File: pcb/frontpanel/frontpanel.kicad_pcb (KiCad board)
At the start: 2 copper layers, 175.8 x 64 mm, 9 parts, among them J1 xx, J2 xx, J3 xx, J4 xx

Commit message: [pcb] update
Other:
- outline, holes or cut-outs redrawn
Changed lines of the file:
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@@
     (property "ki_keywords" "LED diode")
     (attr smd)
-    (fp_text reference "D1" (at 0 1.65) (layer "B.SilkS")
+    (fp_text reference "D1" (at 0 1.8) (layer "B.SilkS")
         (effects (font (size 1 1) (thickness 0.15)) (justify mirror))
     )
@@
     (property "ki_keywords" "LED diode")
     (attr smd)
-    (fp_text reference "D4" (at 0 1.65) (layer "B.SilkS")
+    (fp_text reference "D4" (at 0 1.725) (layer "B.SilkS")
         (effects (font (size 1 1) (thickness 0.15)) (justify mirror))
     )
@@
     (property "ki_keywords" "LED diode")
     (attr smd)
-    (fp_text reference "D3" (at 0 1.65) (layer "B.SilkS")
+    (fp_text reference "D3" (at 0 1.75) (layer "B.SilkS")
         (effects (font (size 1 1) (thickness 0.15)) (justify mirror))
     )
@@
     (property "ki_keywords" "R res resistor")
     (attr smd)
-    (fp_text reference "R1" (at 0 1.43) (layer "B.SilkS")
+    (fp_text reference "R1" (at 0 1.5) (layer "B.SilkS")
         (effects (font (size 1 1) (thickness 0.15)) (justify mirror))
     )
@@
     (property "ki_keywords" "LED diode")
     (attr smd)
-    (fp_text reference "D2" (at 0 1.65) (layer "B.SilkS")
+    (fp_text reference "D2" (at 0 1.725) (layer "B.SilkS")
         (effects (font (size 1 1) (thickness 0.15)) (justify mirror))
     )
@@
   (gr_line (start 215.625 139.094185) (end 73.895815 139.094185)
     (stroke (width 0.05) (type default)) (layer "Edge.Cuts"))
+  (gr_circle (center 97.475 90.8) (end 99.975 90.8)
+    (stroke (width 0.05) (type default)) (fill none) (layer "Edge.Cuts"))
+  (gr_circle (center 193.175 106.75) (end 195.675 106.75)
+    (stroke (width 0.05) (type default)) (fill none) (layer "Edge.Cuts"))
+  (gr_circle (center 97.475 122.8) (end 99.975 122.8)
+    (stroke (width 0.05) (type default)) (fill none) (layer "Edge.Cuts"))
   (gr_arc (start 232.625 122.094185) (mid 227.645821 134.11501) (end 215.625 139.094185)
     (stroke (width 0.05) (type default)) (layer "Edge.Cuts"))
   (gr_arc (start 56.875 92.115) (mid 61.854185 80.094185) (end 73.875 75.115)
     (stroke (width 0.05) (type default)) (layer "Edge.Cuts"))
+  (gr_circle (center 193.375 122.8) (end 195.875 122.8)
+    (stroke (width 0.05) (type default)) (fill none) (layer "Edge.Cuts"))
   (gr_line (start 56.875 92.115) (end 56.895815 122.094185)
     (stroke (width 0.05) (type default)) (layer "Edge.Cuts"))
+  (gr_circle (center 193.175 90.8) (end 195.675 90.8)
+    (stroke (width 0.05) (type default)) (fill none) (layer "Edge.Cuts"))
   (gr_arc (start 215.625 75.115) (mid 227.645815 80.094185) (end 232.625 92.115)
     (stroke (width 0.05) (type default)) (layer "Edge.Cuts"))
+  (gr_circle (center 97.5 106.725) (end 100 106.725)
+    (stroke (width 0.05) (type default)) (fill none) (layer "Edge.Cuts"))
   (gr_rect (start 120.925 94.875) (end 169.525 118.675)
     (stroke (width 0.1) (type default)) (fill none) (layer "Edge.Cuts"))
@@
   )
   (dimension (type aligned) (layer "User.1")
+    (pts (xy 193.275 106.8) (xy 193.275 90.8))
+    (height -13.5)
+    (gr_text "16.0000 mm" (at 178.625 98.8 90) (layer "User.1")
+      (effects (font (size 1 1) (thickness 0.15)))
+    )
+    (format (prefix "") (suffix "") (units 3) (units_format 1) (precision 4))
+    (style (thickness 0.1) (arrow_length 1.27) (text_position_mode 0) (extension_height 0.58642) (extension_offset 0.5) keep_text_aligned)
+  )
+  (dimension (type aligned) (layer "User.1")
     (pts (xy 216.725 82.775) (xy 216.715 106.765))
     (height 169.76259)
@@
   )
   (dimension (type aligned) (layer "User.1")
+    (pts (xy 97.475 122.8) (xy 97.475 106.8))
+    (height -13.5)
+    (gr_text "16.0000 mm" (at 82.825 114.8 90) (layer "User.1")
+      (effects (font (size 1 1) (thickness 0.15)))
+    )
+    (format (prefix "") (suffix "") (units 3) (units_format 1) (precision 4))
+    (style (thickness 0.1) (arrow_length 1.27) (text_position_mode 0) (extension_height 0.58642) (extension_offset 0.5) keep_text_aligned)
+  )
+  (dimension (type aligned) (layer "User.1")
     (pts (xy 73.875 83.115) (xy 81.875 83.115))
     (height -1.75)
@@
   )
   (dimension (type aligned) (layer "User.1")
+    (pts (xy 216.865 106.79) (xy 193.175 106.8))
+    (height 17.469515)
+    (gr_text "23.6900 mm" (at 205.012141 88.175487 0.02418563787) (layer "User.1")
+      (effects (font (size 1 1) (thickness 0.15)))
+    )
+    (format (prefix "") (suffix "") (units 3) (units_format 1) (precision 4))
+    (style (thickness 0.1) (arrow_length 1.27) (text_position_mode 0) (extension_height 0.58642) (extension_offset 0.5) keep_text_aligned)
+  )
+  (dimension (type aligned) (layer "User.1")
     (pts (xy 73.885 131.115) (xy 81.885 131.115))
     (height 3.25)
@@
   )
   (dimension (type aligned) (layer "User.1")
+    (pts (xy 73.875 106.7) (xy 97.475 106.7))
+    (height -5.975)
+    (gr_text "23.6000 mm" (at 85.675 99.575) (layer "User.1")
+      (effects (font (size 1 1) (thickness 0.15)))
+    )
+    (format (prefix "") (suffix "") (units 3) (units_format 1) (precision 4))
+    (style (thickness 0.1) (arrow_length 1.27) (text_position_mode 0) (extension_height 0.58642) (extension_offset 0.5) keep_text_aligned)
+  )
+  (dimension (type aligned) (layer "User.1")
+    (pts (xy 193.275 122.8) (xy 193.275 106.8))
+    (height -13.5)
+    (gr_text "16.0000 mm" (at 178.625 114.8 90) (layer "User.1")
+      (effects (font (size 1 1) (thickness 0.15)))
+    )
+    (format (prefix "") (suffix "") (units 3) (units_format 1) (precision 4))
+    (style (thickness 0.1) (arrow_length 1.27) (text_position_mode 0) (extension_height 0.58642) (extension_offset 0.5) keep_text_aligned)
+  )
+  (dimension (type aligned) (layer "User.1")
     (pts (xy 223.715 82.765) (xy 66.715 82.765))
     (height 20.24)
     (gr_text "157.0000 mm" (at 145.215 61.375) (layer "User.1")
+      (effects (font (size 1 1) (thickness 0.15)))
+    )
+    (format (prefix "") (suffix "") (units 3) (units_format 1) (precision 4))
+    (style (thickness 0.1) (arrow_length 1.27) (text_position_mode 0) (extension_height 0.58642) (extension_offset 0.5) keep_text_aligned)
+  )
+  (dimension (type aligned) (layer "User.1")
+    (pts (xy 97.475 106.8) (xy 97.475 90.8))
+    (height -13.5)
+    (gr_text "16.0000 mm" (at 82.825 98.8 90) (layer "User.1")
       (effects (font (size 1 1) (thickness 0.15)))
     )
@@
     (style (thickness 0.1) (arrow_length 1.27) (text_position_mode 0) (extension_height 0.58642) (extension_offset 0.5) keep_text_aligned)
   )
+  (segment (start 121.578928 120.1) (end 111.575 120.1) (width 0.2) (layer "B.Cu") (net 1))
   (segment (start 83.31 128.075) (end 84.6 128.075) (width 0.2) (layer "B.Cu") (net 1))
+  (segment (start 111.575 120.1) (end 105.275 126.4) (width 0.2) (layer "B.Cu") (net 1))
   (segment (start 83.38 82.8) (end 83.38 128.005) (width 0.2) (layer "B.Cu") (net 1))
   (segment (start 86.65 130.125) (end 206.215 130.125) (width 0.2) (layer "B.Cu") (net 1))
-  (segment (start 121.653928 120.025) (end 91.36 120.025) (width 0.2) (layer "B.Cu") (net 1))
-  (segment (start 91.36 120.025) (end 83.31 128.075) (width 0.2) (layer "B.Cu") (net 1))
+  (segment (start 105.275 126.4) (end 84.985 126.4) (width 0.2) (layer "B.Cu") (net 1))
   (segment (start 84.6 128.075) (end 86.65 130.125) (width 0.2) (layer "B.Cu") (net 1))
   (segment (start 207.46 86.125) (end 207.46 131.37) (width 0.2) (layer "B.Cu") (net 1))
   (segment (start 83.38 128.005) (end 83.31 128.075) (width 0.2) (layer "B.Cu") (net 1))
+  (segment (start 121.653928 120.025) (end 121.578928 120.1) (width 0.2) (layer "B.Cu") (net 1))
   (segment (start 206.215 130.125) (end 207.49 131.4) (width 0.2) (layer "B.Cu") (net 1))
   (segment (start 207.46 131.37) (end 207.49 131.4) (width 0.2) (layer "B.Cu") (net 1))
-  (segment (start 189.68 106.761428) (end 176.366428 120.075) (width 0.2) (layer "B.Cu") (net 19))
-  (segment (start 189.68 82.825) (end 189.68 106.761428) (width 0.2) (layer "B.Cu") (net 19))
+  (segment (start 84.985 126.4) (end 83.31 128.075) (width 0.2) (layer "B.Cu") (net 1))
+  (segment (start 183.9 88.605) (end 183.9 112.541428) (width 0.2) (layer "B.Cu") (net 19))
+  (segment (start 183.9 112.541428) (end 176.366428 120.075) (width 0.2) (layer "B.Cu") (net 19))
+  (segment (start 189.68 82.825) (end 183.9 88.605) (width 0.2) (layer "B.Cu") (net 19))
   (segment (start 174.716428 120.075) (end 168.778928 120.075) (width 0.2) (layer "B.Cu") (net 27))
   (segment (start 133.878928 120.025) (end 123.528928 120.025) (width 0.2) (layer "B.Cu") (net 31))

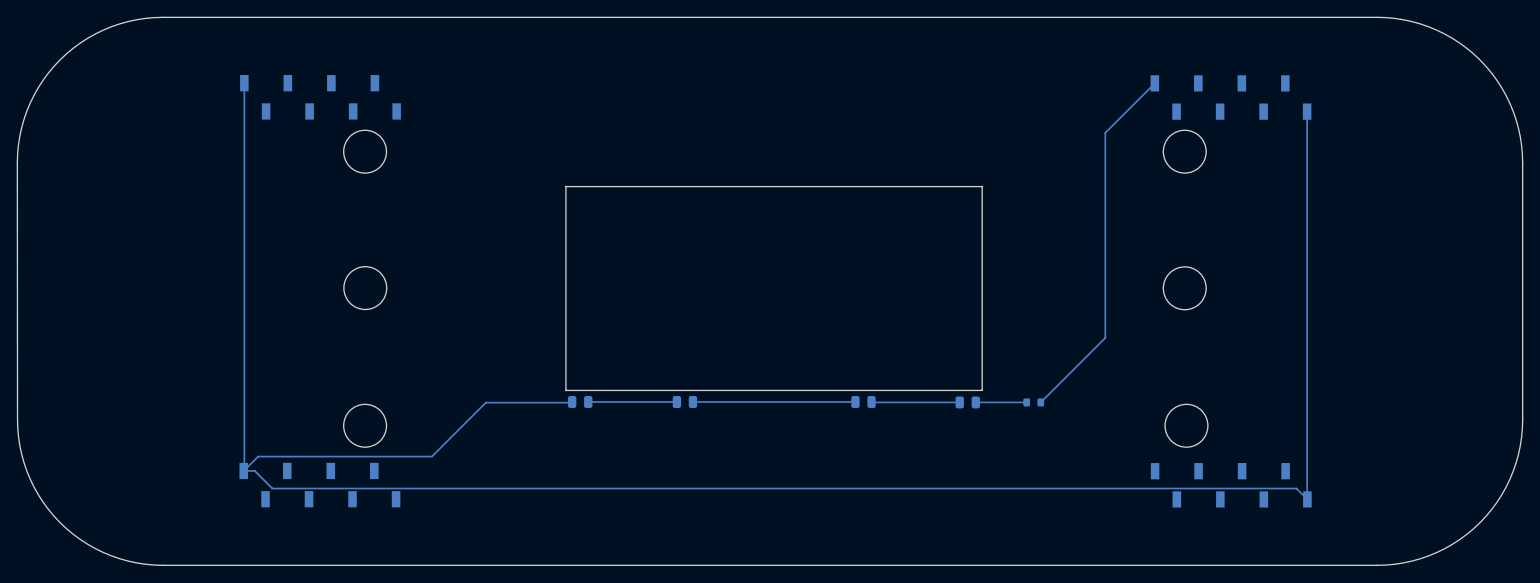
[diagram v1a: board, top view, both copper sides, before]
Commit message: [pcb] update frontpanel (mostly, leds)
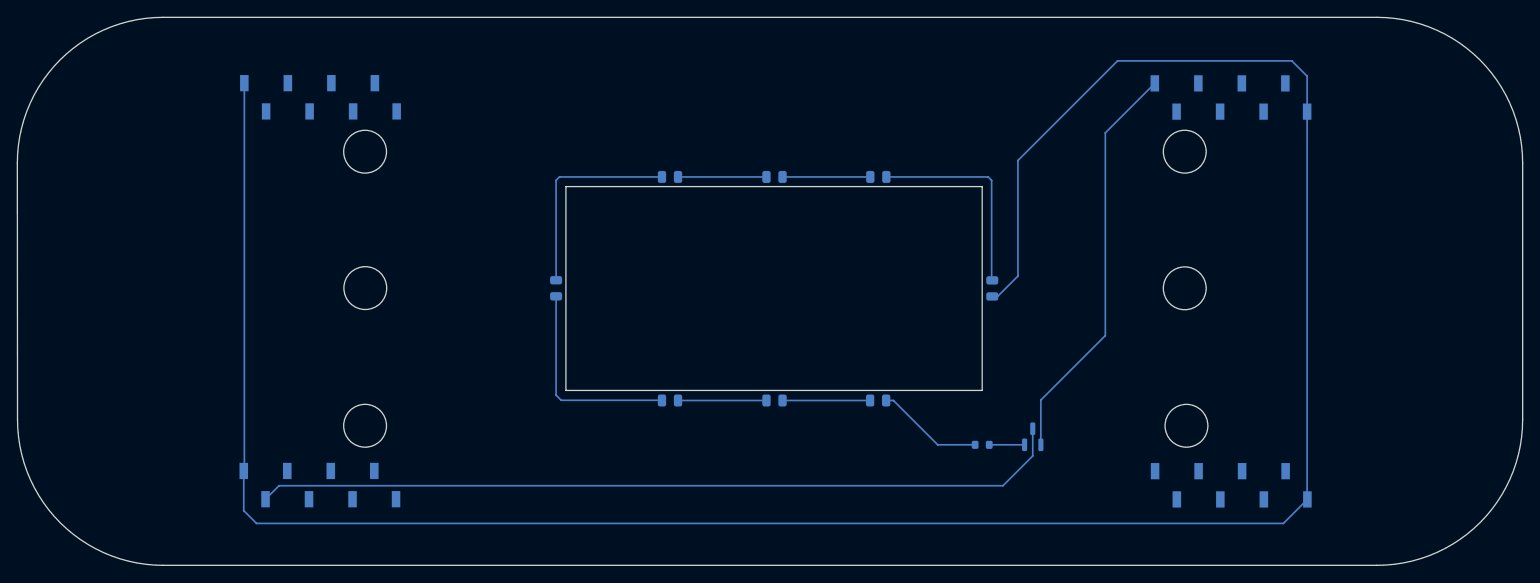
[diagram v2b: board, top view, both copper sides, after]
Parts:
- added D5: LED, LED_SMD:LED_0805_2012Metric, B.Cu at (133.1, 93.8)
- added D6: LED, LED_SMD:LED_0805_2012Metric, B.Cu at (145.3, 93.8)
- added D7: LED, LED_SMD:LED_0805_2012Metric, B.Cu at (157.4, 93.8)
- added D8: LED, LED_SMD:LED_0805_2012Metric, B.Cu at (170.7, 106.8)
- added Q1: NPN, Package_TO_SOT_SMD:SOT-23, B.Cu at (175.4, 124.1)
- moved D1 13.6 mm to (119.8, 106.8), turned to -90 degrees
- moved D4 10.5 mm to (157.4, 119.8)
- moved D3 10.4 mm to (145.3, 119.8)
- moved R1 7.79 mm to (169.5, 125.0)
- moved D2 1.75 mm to (133.1, 119.8)
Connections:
- D1 pad 1: GND -> Net-(D1-K)
- R1 pad 2: GPIO11 -> Net-(Q1-E)
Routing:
- net +3.3V: track 0.00 -> 94.8 mm
- net GND: track 257.8 -> 282.2 mm
- net Net-(D1-K): track 0.00 -> 24.2 mm
- net Net-(D7-K): track 0.00 -> 24.1 mm
- net Net-(D1-A): track 10.4 -> 24.2 mm
- net Net-(D5-K): track 0.00 -> 10.3 mm
- net Net-(D6-K): track 0.00 -> 10.2 mm
- net Net-(D2-A): track 19.0 -> 10.3 mm
- net Net-(D4-A): track 5.94 -> 12.5 mm
- net GPIO11: track 42.8 -> 47.7 mm
- net Net-(Q1-E): track 0.00 -> 4.12 mm

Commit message: [pcb] fix frontpanel pcb LEDs + connexion to main pcb
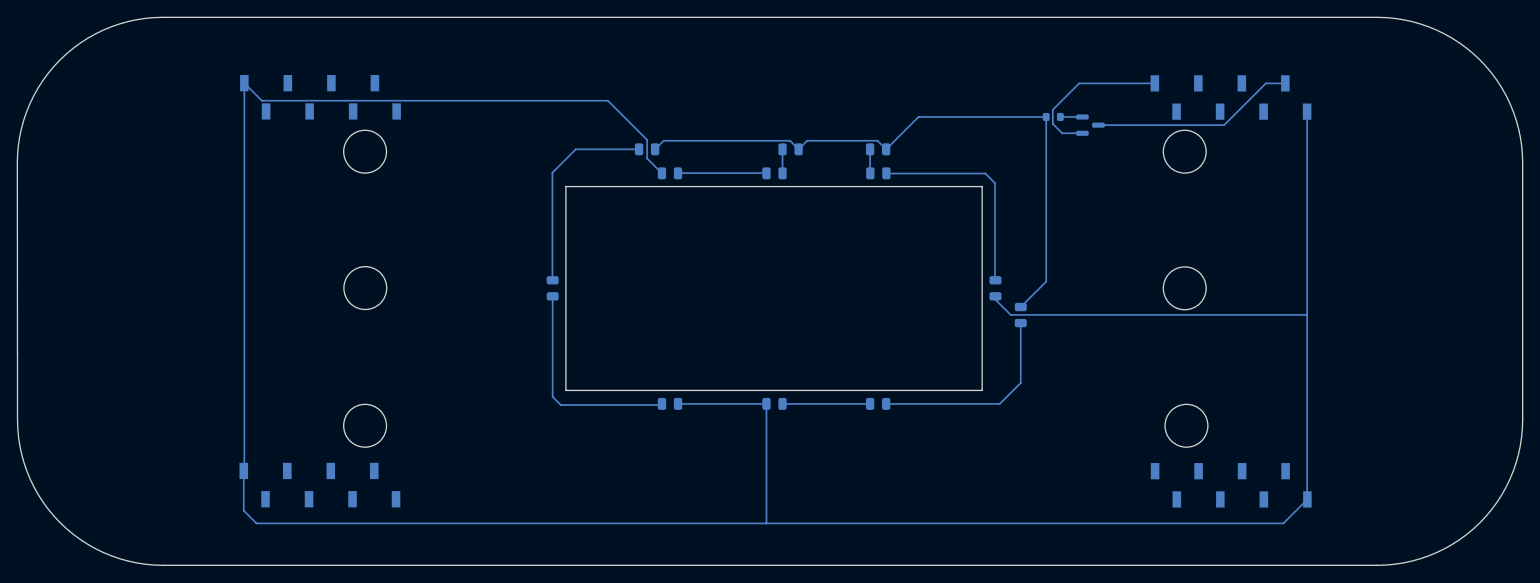
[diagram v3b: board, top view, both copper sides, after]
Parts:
- added F1: Fuse, Fuse:Fuse_0805_2012Metric, B.Cu at (130.4, 90.5)
- added F2: Fuse, Fuse:Fuse_0805_2012Metric, B.Cu at (157.4, 90.5)
- added F3: Fuse, Fuse:Fuse_0805_2012Metric, B.Cu at (147.2, 90.5)
- added F4: Fuse, Fuse:Fuse_0805_2012Metric, B.Cu at (174.0, 109.9)
- moved R1 39.2 mm to (177.8, 86.8)
- moved Q1 37.0 mm to (182.2, 87.7), turned to 0 degrees
- moved D5 0.42 mm to (133.1, 93.3), turned to 0 degrees
- moved D6 0.42 mm to (145.3, 93.3), turned to 0 degrees
- moved D7 0.42 mm to (157.4, 93.3)
- moved D1 0.40 mm to (119.4, 106.8), turned to 90 degrees
- moved D2 0.40 mm to (133.1, 120.2), turned to 180 degrees
- moved D3 0.40 mm to (145.3, 120.2)
- moved D4 0.40 mm to (157.4, 120.2)
- moved D8 0.38 mm to (171.1, 106.8)
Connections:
- D2 pad 1: Net-(D1-A) -> GND
- D2 pad 2: Net-(D2-A) -> Net-(D1-K)
- D3 pad 1: Net-(D2-A) -> GND
- D5 pad 1: Net-(D5-K) -> GND
- D5 pad 2: Net-(D1-K) -> Net-(D5-A)
- D6 pad 1: Net-(D6-K) -> Net-(D5-A)
- D6 pad 2: Net-(D5-K) -> Net-(D6-A)
- D7 pad 2: Net-(D6-K) -> Net-(D7-A)
- J1 pad 2: unconnected-(J1-Pin_2-Pad2) -> +5V
- J1 pad 3: unconnected-(J1-Pin_3-Pad3) -> +3.3V
- J3 pad 2: +3.3V -> unconnected-(J3-Pin_2-Pad2)
- Q1 pad 3: +3.3V -> +5V
- R1 pad 1: Net-(D4-A) -> Net-(F1-Pad1)
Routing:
- net +3.3V: track 94.8 -> 0.00 mm
- net Net-(F1-Pad1): track 0.00 -> 72.3 mm
- net GND: track 282.2 -> 337.4 mm
- net GPIO11: track 47.7 -> 18.7 mm
- net +5V: track 0.00 -> 23.8 mm
- net Net-(D4-A): track 12.5 -> 23.7 mm
- net Net-(D5-A): track 0.00 -> 10.3 mm
- net Net-(D5-K): track 10.3 -> 0.00 mm
- net Net-(D2-A): track 10.3 -> 0.00 mm
- net Net-(D6-K): track 10.2 -> 0.00 mm
- net Net-(D7-A): track 0.00 -> 3.24 mm
- net Net-(D6-A): track 0.00 -> 2.80 mm
- net Net-(Q1-E): track 4.12 -> 2.57 mm
- net Net-(D1-K): track 24.2 -> 24.9 mm

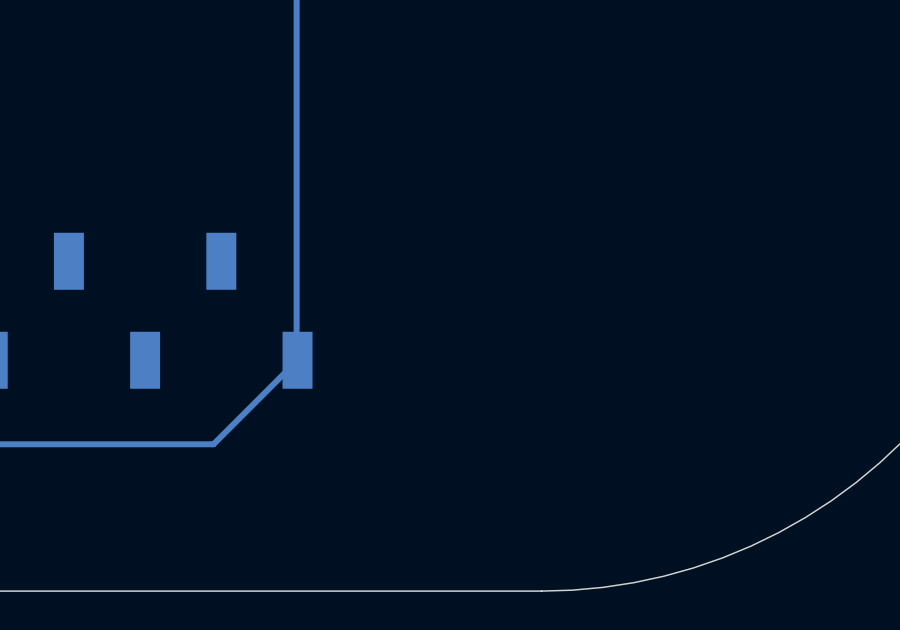
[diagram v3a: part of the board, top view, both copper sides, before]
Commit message: [pcb] add capybara logo
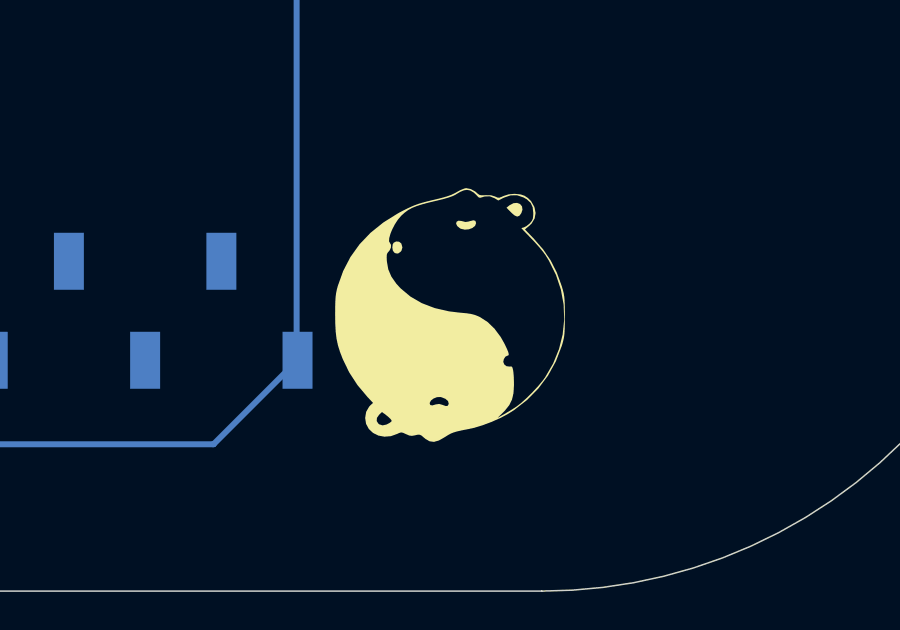
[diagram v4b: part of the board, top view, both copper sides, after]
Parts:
- added G***: LOGO, capybara:capybara, F.Cu at (212.7, 129.6)
